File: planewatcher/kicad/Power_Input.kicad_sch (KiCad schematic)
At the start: 3 parts

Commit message: Add persistent PCBWay BOM fields to KiCad schematic
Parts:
- D2: MPN (none) -> TPD1E10B06DYAR; Manufacturer (none) -> Texas Instruments; Package (none) -> SMB
- F1: MPN (none) -> 1812L110/24DR; Manufacturer (none) -> Littelfuse; Package (none) -> 1812
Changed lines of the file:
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@@
+			)
+		)
+		(property "Package" "SMB"
+			(at 111.76 96.52 0)
+			(hide yes)
+			(show_name no)
+			(do_not_autoplace no)
+			(effects
+				(font
+					(size 1.27 1.27)
+				)
+			)
+		)
+		(property "MPN" "TPD1E10B06DYAR"
+			(at 111.76 96.52 0)
+			(hide yes)
+			(show_name no)
+			(do_not_autoplace no)
+			(effects
+				(font
+					(size 1.27 1.27)
+				)
+			)
+		)
+		(property "Manufacturer" "Texas Instruments"
+			(at 111.76 96.52 0)
+			(hide yes)
+			(show_name no)
+			(do_not_autoplace no)
+			(effects
+				(font
+					(size 1.27 1.27)
+				)
 			)
 		)
@@
 			(at 100.33 88.9 0)
 			(hide yes)
+			(show_name no)
+			(do_not_autoplace no)
+			(effects
+				(font
+					(size 1.27 1.27)
+				)
+			)
+		)
+		(property "Package" "1812"
+			(at 100.33 88.9 0)
+			(hide yes)
+			(show_name no)
+			(do_not_autoplace no)
+			(effects
+				(font
+					(size 1.27 1.27)
+				)
+			)
+		)
+		(property "MPN" "1812L110/24DR"
+			(at 100.33 88.9 0)
+			(hide yes)
+			(show_name no)
+			(do_not_autoplace no)
+			(effects
+				(font
+					(size 1.27 1.27)
+				)
+			)
+		)
+		(property "Manufacturer" "Littelfuse"
+			(at 100.33 88.9 0)
+			(hide yes)

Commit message: move power supply and add GPS module
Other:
- title: Plane Watcher: Power Input Protection & Filtering -> Plane Watcher
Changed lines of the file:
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@@
 	(paper "A4")
 	(title_block
-		(title "Plane Watcher: Power Input Protection & Filtering")
-		(date "2026-05-16")
-		(rev "prototype 1.1")
+		(title "Plane Watcher")
+		(date "2026-05-18")
+		(rev "prototype 1.2")
 		(company "plane.watch")
 	)

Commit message: review & consolidate all capacitors
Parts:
- D2: Suggested Part Texas Instruments TPD1E10B06DYAR -> (none)
- F1: Suggested Part Littelfuse 1812L110/24DR -> (none)
- TP20: Suggested Part No fitted part (PCB pad only) -> (none)
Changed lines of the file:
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@@
-			)
-		)
-		(property "Suggested Part" "Texas Instruments TPD1E10B06DYAR"
-			(at 111.76 96.52 0)
-			(hide yes)
-			(show_name no)
-			(do_not_autoplace no)
-			(effects
-				(font
-					(size 1.27 1.27)
-				)
 			)
 		)
 		(property "Purpose" "Clamps input supply transients on the protected power input."
 			(at 111.76 96.52 0)
+			(hide yes)
+			(show_name no)
+			(do_not_autoplace no)
+			(effects
+				(font
+					(size 1.27 1.27)
+				)
+			)
+		)
+		(property "Mount_Type" ""
+			(at 111.76 96.52 90)
 			(hide yes)
 			(show_name no)
@@
 			)
 		)
-		(property "Suggested Part" "No fitted part (PCB pad only)"
+		(property "Purpose" "Provides oscilloscope/DMM probe access to V+."
 			(at 129.54 96.52 0)
 			(hide yes)
@@
 			)
 		)
-		(property "Purpose" "Provides oscilloscope/DMM probe access to V+."
+		(property "Mount_Type" ""
 			(at 129.54 96.52 0)
 			(hide yes)
@@
 			)
 		)
-		(property "Suggested Part" "Littelfuse 1812L110/24DR"
-			(at 100.33 88.9 0)
-			(hide yes)
-			(show_name no)
-			(do_not_autoplace no)
-			(effects
-				(font
-					(size 1.27 1.27)
-				)
-			)
-		)
 		(property "Purpose" "Provides resettable overcurrent protection at the board power input."
 			(at 100.33 88.9 0)
 			(hide yes)
 			(show_name no)
+			(do_not_autoplace no)
+			(effects
+				(font
+					(size 1.27 1.27)
+				)
+			)
+		)
+		(property "Mount_Type" ""
+			(at 100.33 88.9 90)
+			(hide yes)
+			(show_name no)

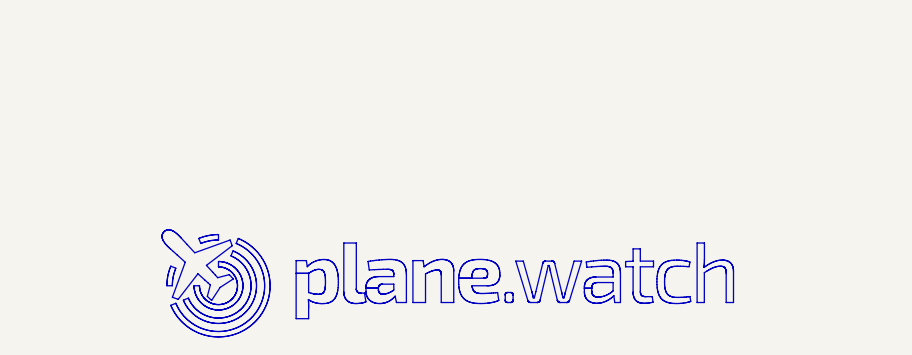
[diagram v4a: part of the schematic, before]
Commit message: add license & copyright info to schematic and pcb. fix layer window.
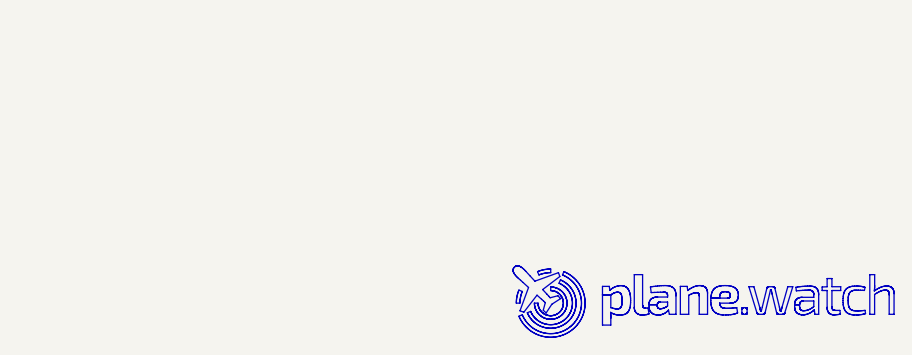
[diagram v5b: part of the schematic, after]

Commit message: added lcsc_ids to all parts
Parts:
- D2: lcsc_id (none) -> C3712135
- F1: lcsc_id (none) -> C207066
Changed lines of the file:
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@@
+			)
+		)
+		(property "lcsc_id" "C3712135"
+			(at 111.76 96.52 0)
+			(hide yes)
+			(show_name no)
+			(do_not_autoplace no)
+			(effects
+				(font
+					(size 1.27 1.27)
+				)
 			)
 		)
@@
 			(at 100.33 88.9 0)
 			(hide yes)
+			(show_name no)
+			(do_not_autoplace no)
+			(effects
+				(font
+					(size 1.27 1.27)
+				)
+			)
+		)
+		(property "lcsc_id" "C207066"
+			(at 100.33 88.9 0)
+			(hide yes)
